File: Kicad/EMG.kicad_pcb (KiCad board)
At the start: 2 copper layers, 32 x 35 mm, 46 parts, among them IC1 MAX8881EUT33-T, P1 nRF24l01, P2 CONN_01X02, P3 USB_A, P4 CONN_01X05, P5 CONN_01X03, SW1 SW_PUSH, U1 MSP430G2231IPW14, U2 TLC2274, U3 TLC2274, U4 MCP73831

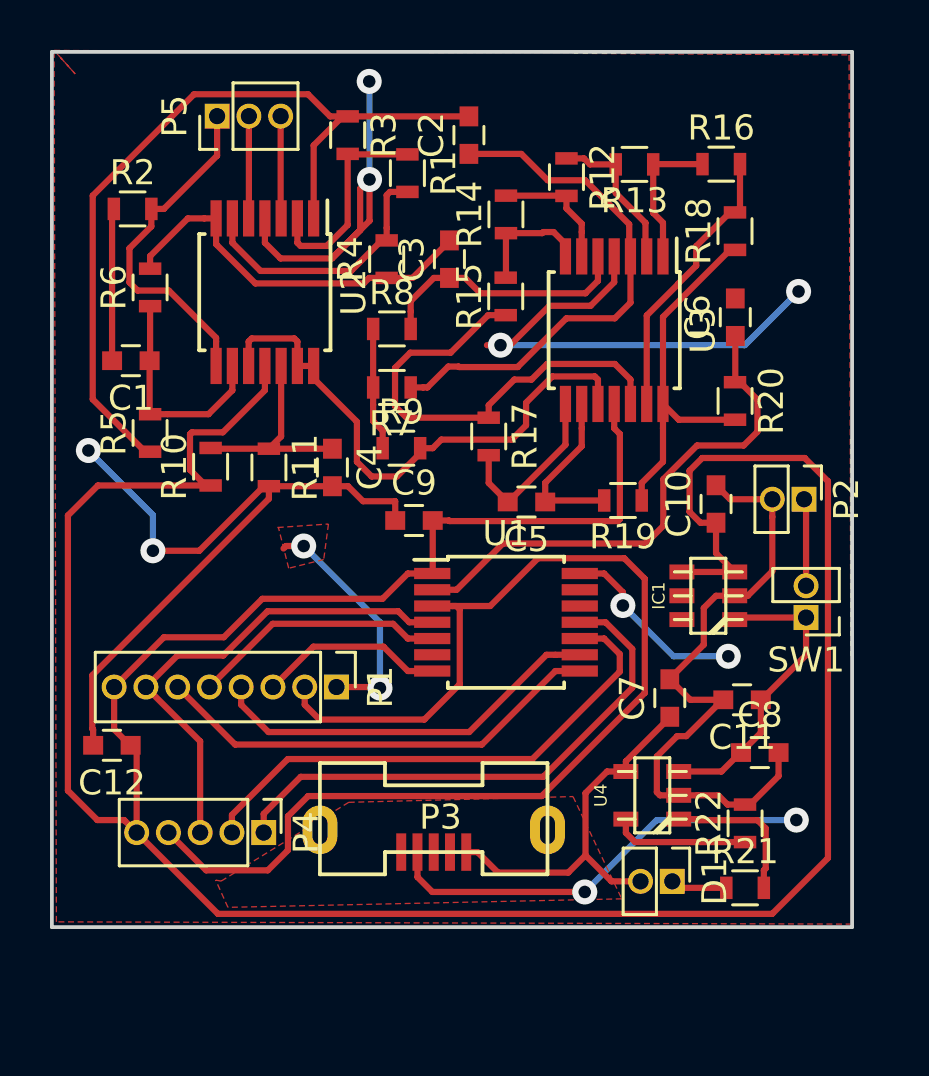
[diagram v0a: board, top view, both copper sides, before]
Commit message: Cambiado el switch por uno de punto medio. Aumento de ancho en pistas de alimentación. Plano de masa
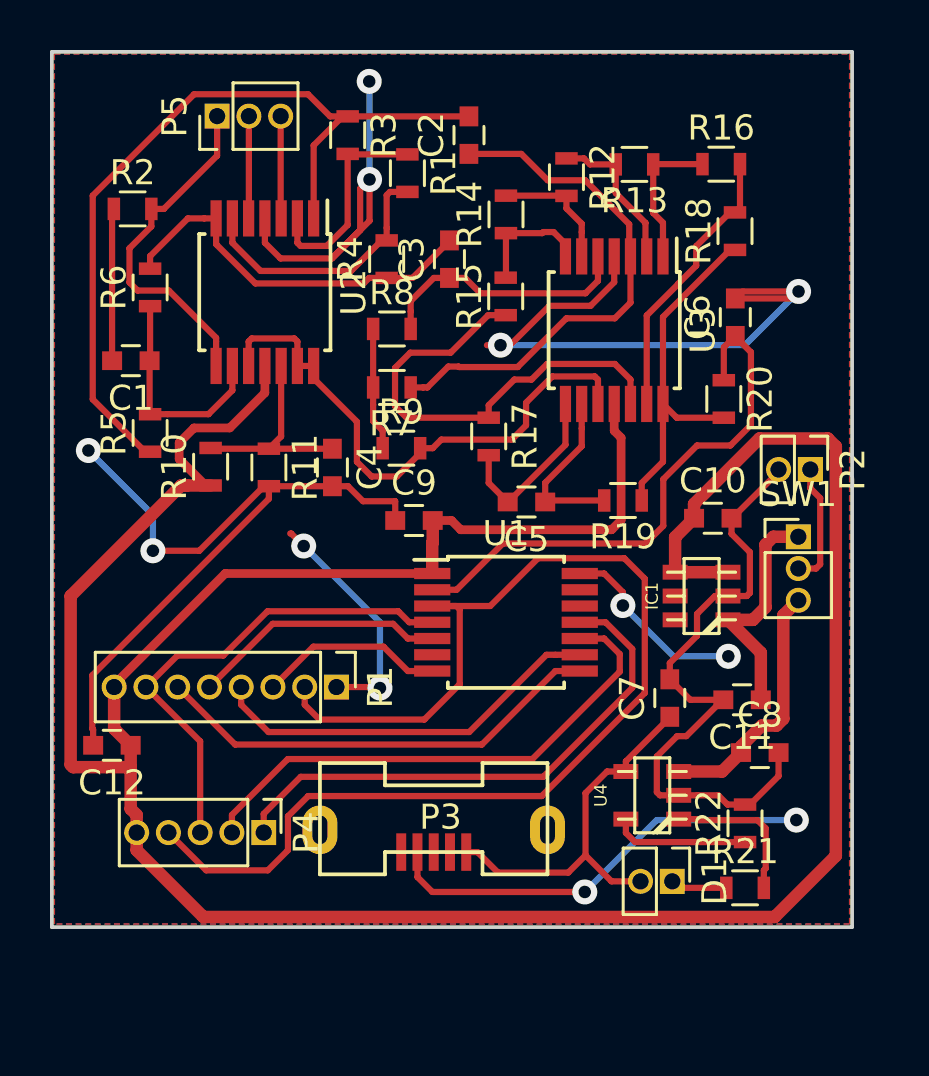
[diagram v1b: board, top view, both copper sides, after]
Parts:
- SW1: value SW_PUSH -> SWITCH_INV; footprint EMG:Pin_Header_Straight_1x02_Pitch1.27mm -> EMG:Pin_Header_Straight_1x03_Pitch1.27mm
- moved SW1 3.24 mm to (169.8, 138.5), turned to 0 degrees
- moved P2 1.22 mm to (170.3, 135.8)
- moved C10 0.58 mm to (166.4, 137.8), turned to 0 degrees
- moved R20 0.46 mm to (166.9, 133.0)
- moved IC1 0.27 mm to (166.0, 140.9)
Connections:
- C8 pad 1: +BATT -> VDD
- U4 pad 3: +BATT -> VDD
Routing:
- net VDD: track 0.00 -> 10.2 mm
- net GND: track 126.4 -> 130.6 mm
- net +BATT: track 12.2 -> 9.43 mm
- net VCC: track 121.6 -> 119.0 mm
- net Net-(P2-Pad1): track 3.49 -> 4.90 mm
- net /Microcontrolador/ADCin: track 21.0 -> 22.3 mm
- added copper zone on B.Cu, net GND

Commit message: Se creó el footprint usb_vert_2, y se cambió el pin out del usb en el esquema
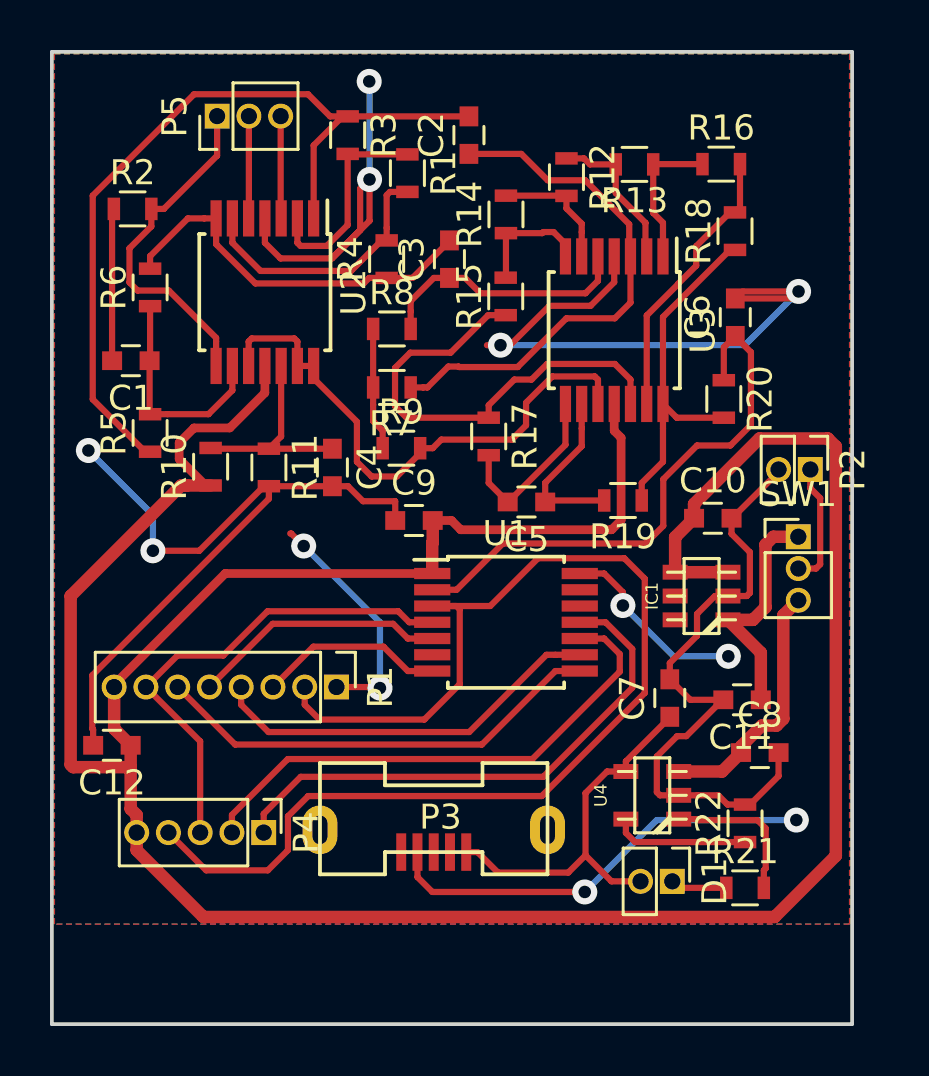
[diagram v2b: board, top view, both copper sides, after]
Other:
- board size 32 x 35 mm -> 32 x 38.9 mm
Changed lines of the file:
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@@
-(kicad_pcb (version 4) (host pcbnew 4.0.2-stable)
+(kicad_pcb (version 4) (host pcbnew 4.0.4-stable)
   (general
     (links 100)
     (no_connects 0)
-    (area 139.924999 119.044999 172.075001 154.195001)
+    (area 139.71 116.605897 174.361905 161.945001)
     (thickness 1.6)
     (drawings 4)
@@
     (pad 7 thru_hole oval (at -4.55 0.89 180) (size 1.4 1.95) (drill oval 0.6 1.15) (layers *.Cu *.Mask))
   )
-  (gr_line (start 140 154.12) (end 140 119.12) (layer Edge.Cuts) (width 0.15))
-  (gr_line (start 172 154.12) (end 140 154.12) (layer Edge.Cuts) (width 0.15))
-  (gr_line (start 172 119.12) (end 172 154.12) (layer Edge.Cuts) (width 0.15))
+  (gr_line (start 140 158) (end 140 119.12) (layer Edge.Cuts) (width 0.15))
+  (gr_line (start 172 158) (end 140 158) (layer Edge.Cuts) (width 0.15))
+  (gr_line (start 172 119.12) (end 172 158) (layer Edge.Cuts) (width 0.15))
   (gr_line (start 140 119.12) (end 172 119.12) (layer Edge.Cuts) (width 0.15))
   (segment (start 147.217709 131.679231) (end 147.217709 132.654231) (width 0.25) (layer F.Cu) (net 1))

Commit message: Se cambió el footprint del usb.
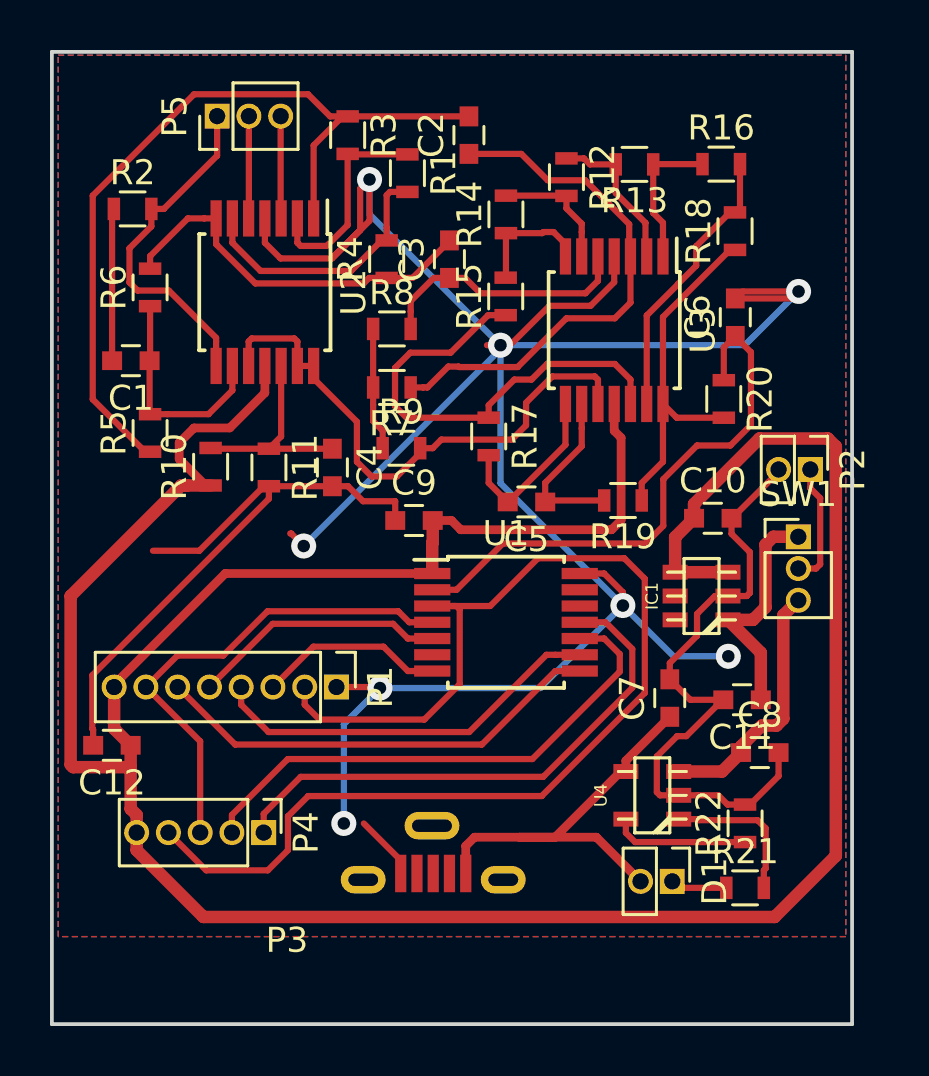
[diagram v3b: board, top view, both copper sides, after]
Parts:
- P3: value USB_A -> MICRO_USB_B; footprint EMG:usb_vert -> EMG:usb_vert_2
- moved P3 0.86 mm to (155.2, 152.0)
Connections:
- P3 pad 4: GND -> Net-(P3-Pad4)
- P3 pad 5: Net-(P3-Pad5) -> GND
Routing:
- net GND: track 130.6 -> 149.3 mm, vias 12 -> 8
- net Net-(C7-Pad1): track 15.8 -> 17.2 mm
